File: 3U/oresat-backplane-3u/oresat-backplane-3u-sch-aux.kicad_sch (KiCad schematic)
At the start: 0 parts

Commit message: Added example aux connectors.
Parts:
- added CF2.1, CF3.1: SFM-110-01-S-D-LC, oresat-connectors:J-SAMTEC-CF-SFM-110-X1-XXX-D-LC, symbol oresat-connectors:J-SAMTEC-SFM-110-X1-XXX-D-LC
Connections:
- new net GND: CF2.1.LC1, CF2.1.LC2, CF3.1.LC1, CF3.1.LC2
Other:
- note added: "All capacitors 0603 >= 25V unless otherwise noted. All resistors 0603 1% unelss otherwise noted."
- note added: "NOTE: Aux connector is the Samtec SFM-110, which has an infinite variety of versions. For a discussion on those varieties, see"

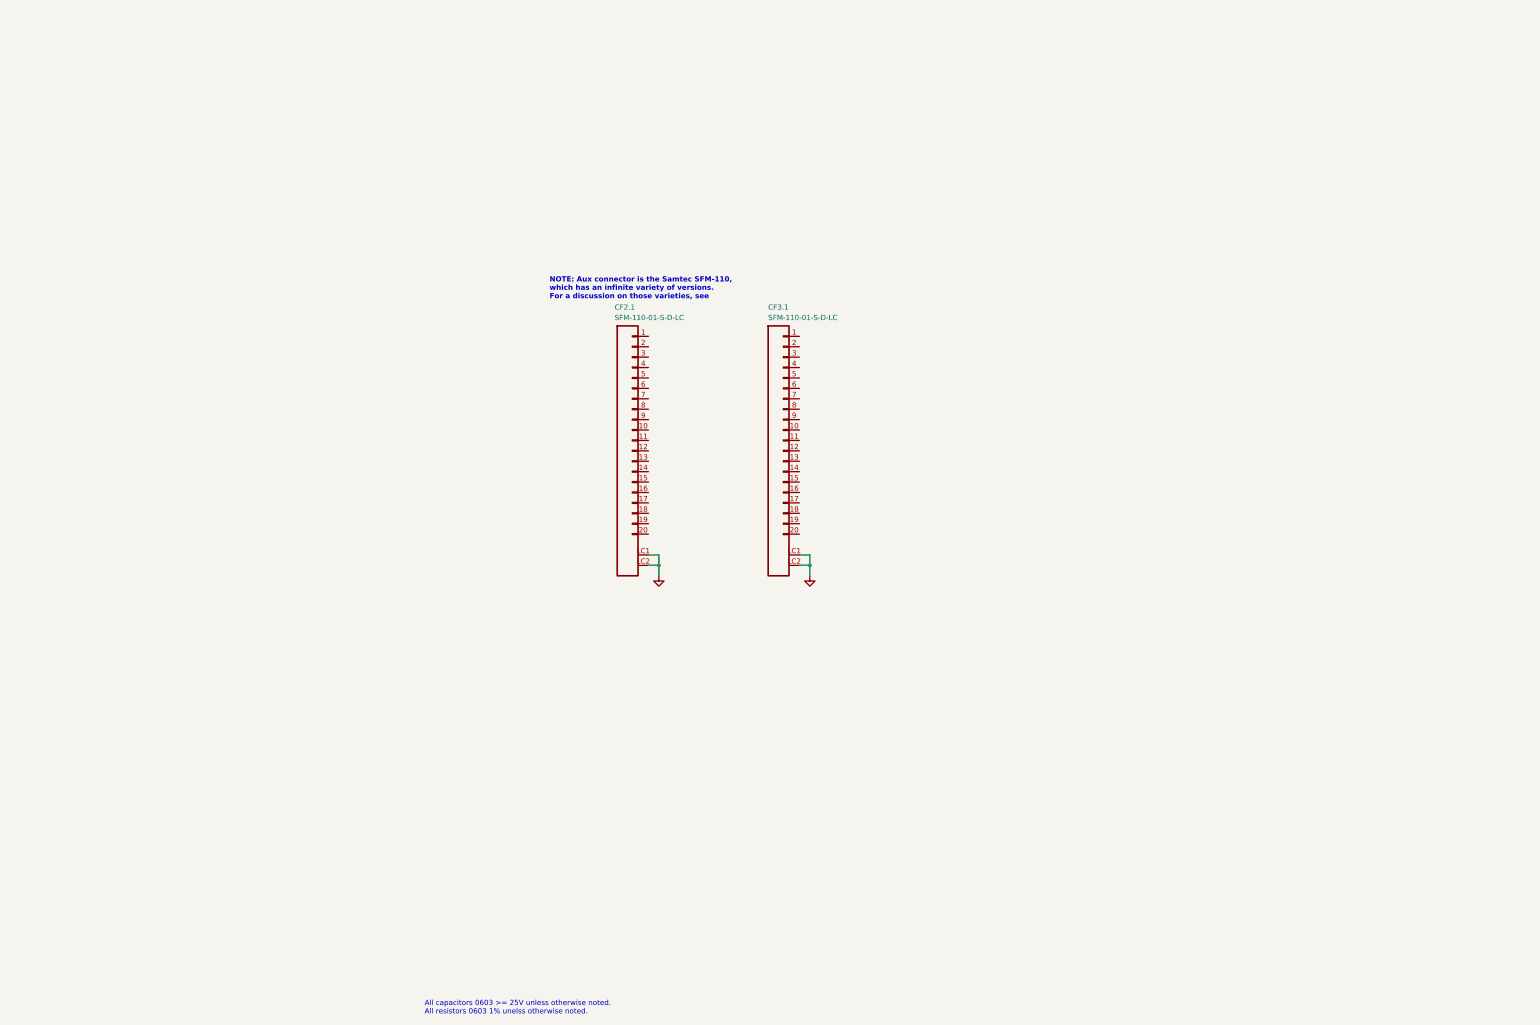
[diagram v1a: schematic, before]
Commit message: Added more Auxiliary connectors
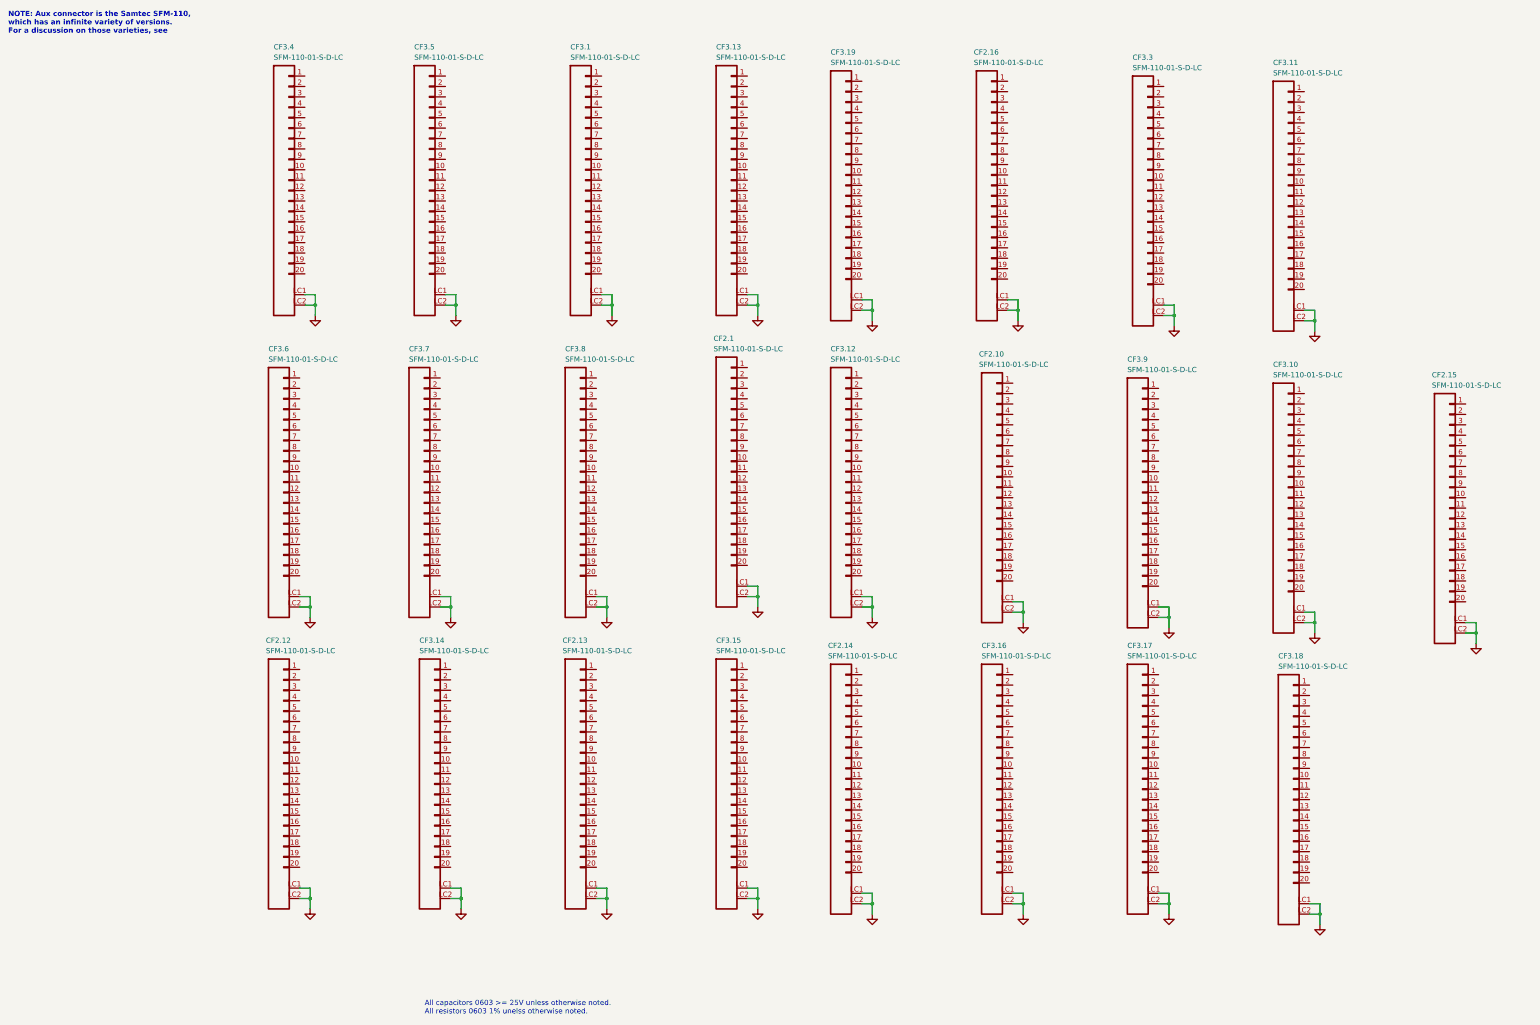
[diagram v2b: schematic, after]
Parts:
- added CF2.10, CF2.12, CF2.13, CF2.14, CF2.15, CF2.16, CF3.10, CF3.11, CF3.12, CF3.13, CF3.14, CF3.15, CF3.16, CF3.17, CF3.18, CF3.19, CF3.3, CF3.4, CF3.5, CF3.6, CF3.7, CF3.8, CF3.9: SFM-110-01-S-D-LC, oresat-connectors:J-SAMTEC-CF-SFM-110-X1-XXX-D-LC, symbol oresat-connectors:J-SAMTEC-SFM-110-X1-XXX-D-LC
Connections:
- net GND: now also CF2.10.LC1, CF2.10.LC2, CF2.12.LC1, CF2.12.LC2, CF2.13.LC1, CF2.13.LC2, CF2.14.LC1, CF2.14.LC2, CF2.15.LC1, CF2.15.LC2, CF2.16.LC1, CF2.16.LC2, CF3.10.LC1, CF3.10.LC2, CF3.11.LC1, CF3.11.LC2, CF3.12.LC1, CF3.12.LC2, CF3.13.LC1, CF3.13.LC2, CF3.14.LC1, CF3.14.LC2, CF3.15.LC1, CF3.15.LC2, CF3.16.LC1, CF3.16.LC2, CF3.17.LC1, CF3.17.LC2, CF3.18.LC1, CF3.18.LC2, CF3.19.LC1, CF3.19.LC2, CF3.3.LC1, CF3.3.LC2, CF3.4.LC1, CF3.4.LC2, CF3.5.LC1, CF3.5.LC2, CF3.6.LC1, CF3.6.LC2, CF3.7.LC1, CF3.7.LC2, CF3.8.LC1, CF3.8.LC2, CF3.9.LC1, CF3.9.LC2
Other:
- moved on the sheet: CF2.1, CF3.1

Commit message: Connectors laid out, unrouted
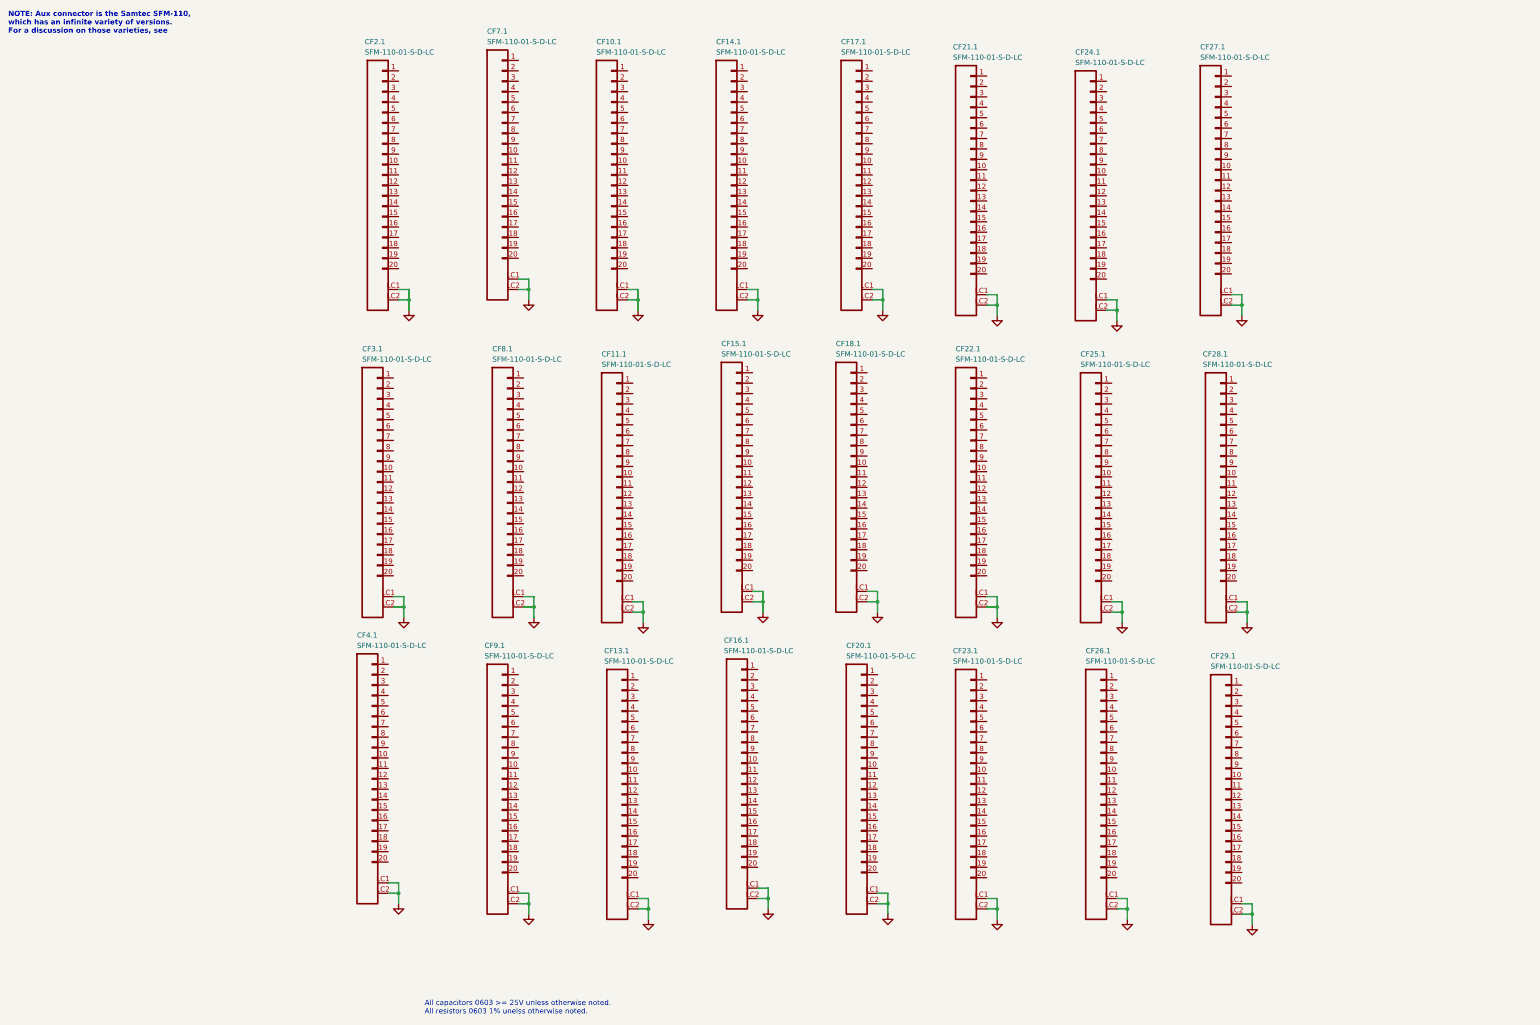
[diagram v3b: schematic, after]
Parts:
- removed CF3.14, CF3.17, CF3.18, CF3.6, CF3.7: SFM-110-01-S-D-LC, oresat-connectors:J-SAMTEC-CF-SFM-110-X1-XXX-D-LC, symbol oresat-connectors:J-SAMTEC-SFM-110-X1-XXX-D-LC
- added CF10.1, CF22.1, CF29.1, CF4.1: SFM-110-01-S-D-LC, oresat-connectors:J-SAMTEC-CF-SFM-110-X1-XXX-D-LC, symbol oresat-connectors:J-SAMTEC-SFM-110-X1-XXX-D-LC
- renumbered CF3.4 to CF11.1, CF2.13 to CF13.1, CF3.5 to CF14.1, CF3.8 to CF15.1, CF2.14 to CF16.1, CF3.13 to CF17.1, CF3.12 to CF18.1, CF3.19 to CF20.1, CF2.10 to CF21.1, CF2.16 to CF23.1, CF3.9 to CF24.1, CF3.10 to CF25.1, CF3.3 to CF26.1, CF3.11 to CF27.1, CF2.15 to CF28.1, CF3.15 to CF7.1, CF3.16 to CF8.1, CF2.12 to CF9.1
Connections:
- net GND: now also CF10.1.LC1, CF10.1.LC2, CF22.1.LC1, CF22.1.LC2, CF29.1.LC1, CF29.1.LC2, CF4.1.LC1, CF4.1.LC2
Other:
- moved on the sheet: CF11.1, CF13.1, CF14.1, CF15.1, CF16.1, CF17.1, CF18.1, CF2.1, CF20.1, CF21.1, CF23.1, CF24.1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

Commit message: Moved can lines to back & fixed RF schematic organization
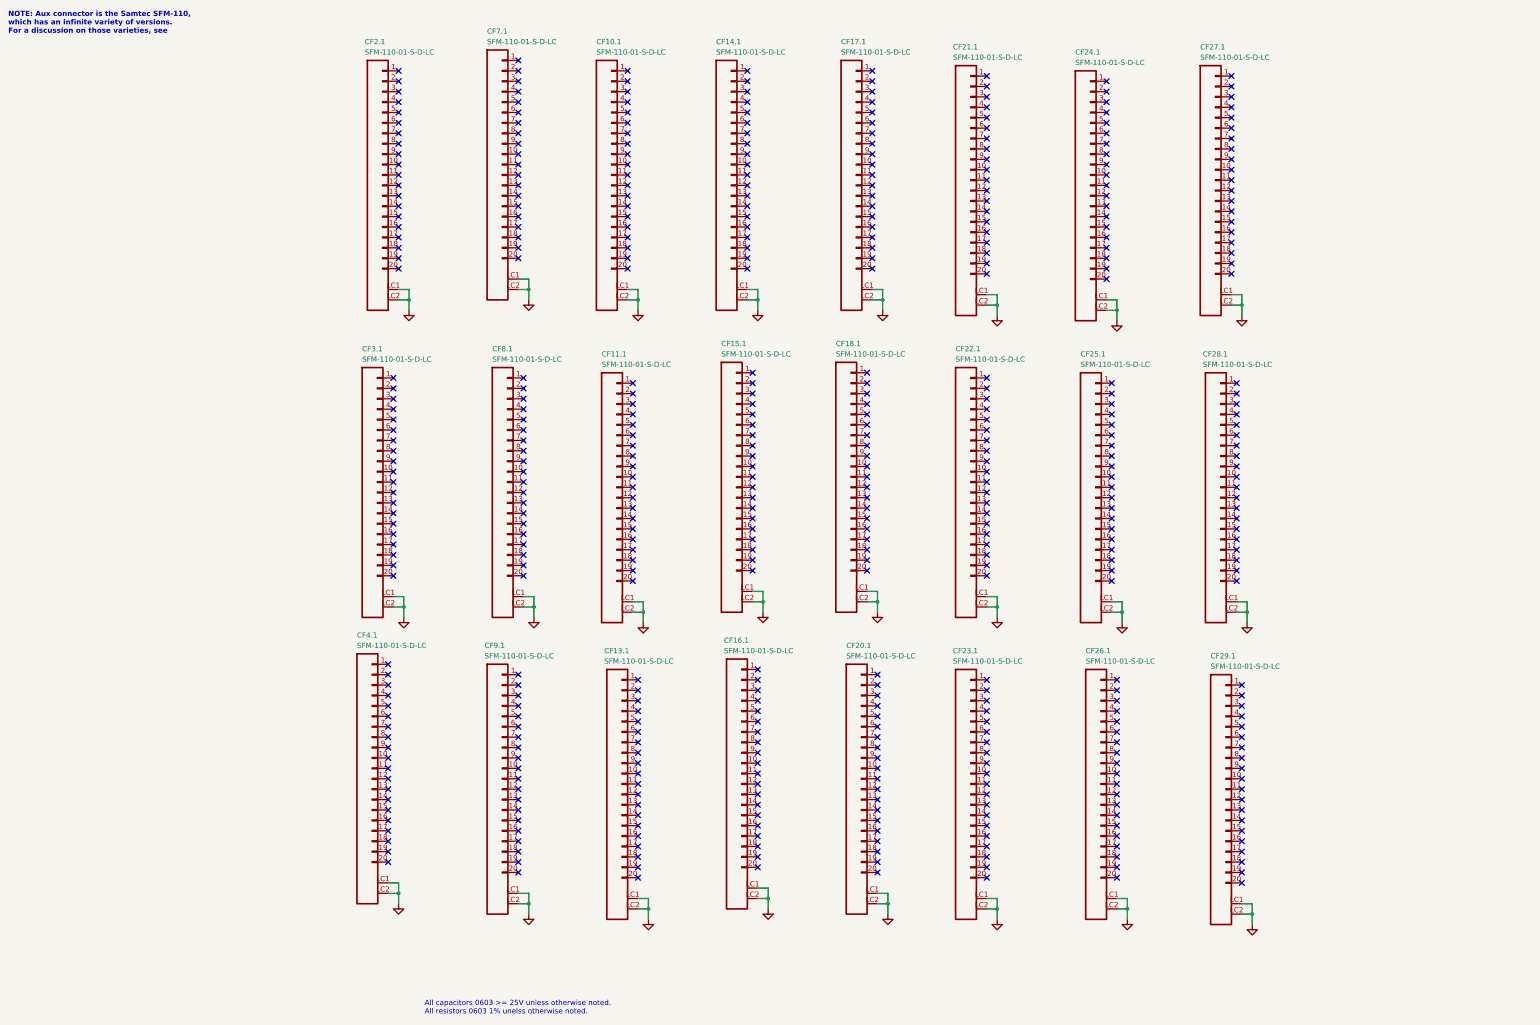
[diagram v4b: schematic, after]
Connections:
- no-connect marks 0 -> 480

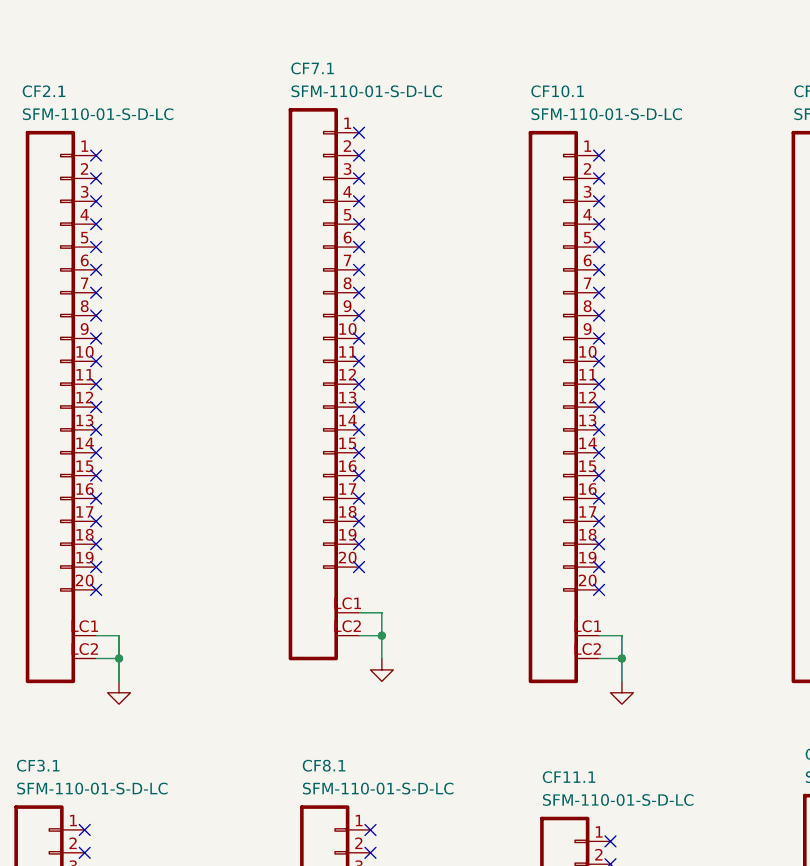
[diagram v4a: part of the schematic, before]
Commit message: Back solder mask added & can resistors moved to F.cu. Final
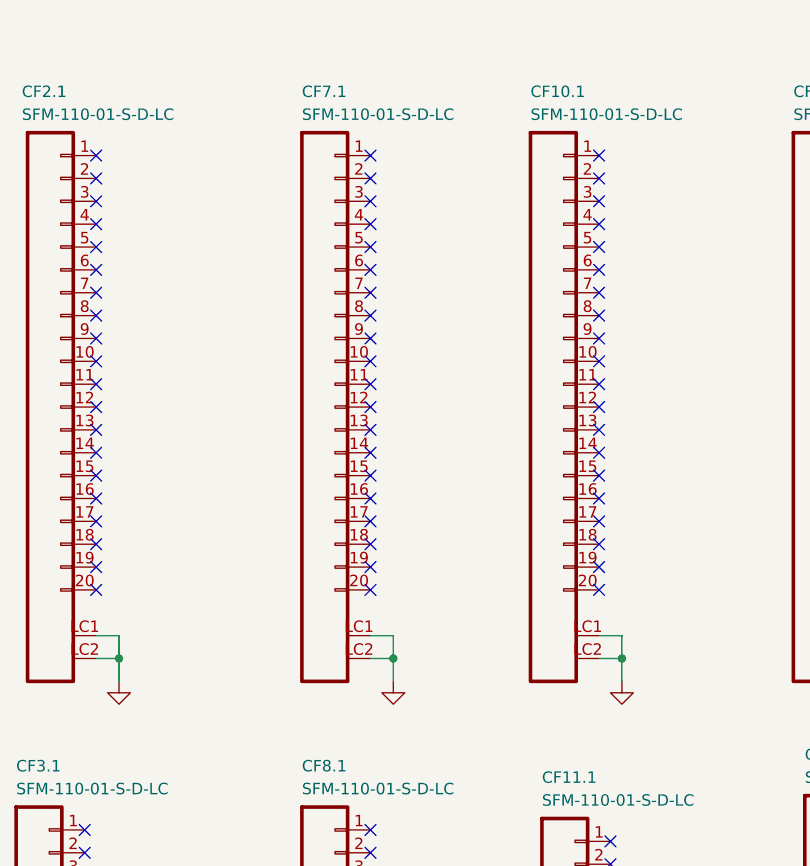
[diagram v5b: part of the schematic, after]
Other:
- moved on the sheet: CF7.1
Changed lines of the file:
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@@
 	)
 	(junction
-		(at 146.05 91.44)
+		(at 147.32 93.98)
 		(diameter 0)
 		(color 0 0 0 0)
@@
 	)
 	(no_connect
-		(at 143.51 53.34)
+		(at 144.78 55.88)
 	)
 	(no_connect
@@
 	)
 	(no_connect
-		(at 143.51 48.26)
+		(at 144.78 50.8)
 	)
 	(no_connect
@@
 	)
 	(no_connect
-		(at 143.51 81.28)
+		(at 144.78 83.82)
 	)
 	(no_connect
@@
 	)
 	(no_connect
-		(at 143.51 63.5)
+		(at 144.78 66.04)
 	)
 	(no_connect
@@
 	)
 	(no_connect
-		(at 143.51 78.74)
+		(at 144.78 81.28)
 	)
 	(no_connect
@@
 	)
 	(no_connect
-		(at 143.51 35.56)
+		(at 144.78 38.1)
 	)
 	(no_connect
@@
 	)
 	(no_connect
-		(at 143.51 66.04)
+		(at 144.78 68.58)
 	)
 	(no_connect
@@
 	)
 	(no_connect
-		(at 143.51 55.88)
+		(at 144.78 58.42)
 	)
 	(no_connect
@@
 	)
 	(no_connect
-		(at 143.51 60.96)
+		(at 144.78 63.5)
 	)
 	(no_connect
-		(at 143.51 38.1)
+		(at 144.78 40.64)
 	)
 	(no_connect
@@
 	)
 	(no_connect
-		(at 143.51 43.18)
+		(at 144.78 45.72)
 	)
 	(no_connect
@@
 	)
 	(no_connect
-		(at 143.51 40.64)
+		(at 144.78 43.18)
 	)
 	(no_connect
@@
 	)
 	(no_connect
-		(at 143.51 71.12)
+		(at 144.78 73.66)
 	)
 	(no_connect
@@
 	)
 	(no_connect
-		(at 143.51 45.72)
+		(at 144.78 48.26)
 	)
 	(no_connect
@@
 	)
 	(no_connect
-		(at 143.51 73.66)
+		(at 144.78 76.2)
 	)
 	(no_connect
@@
 	)
 	(no_connect
-		(at 143.51 50.8)
+		(at 144.78 53.34)
 	)
 	(no_connect
@@
 	)
 	(no_connect
-		(at 143.51 58.42)
+		(at 144.78 60.96)
 	)
 	(no_connect
@@
 	)
 	(no_connect
-		(at 143.51 68.58)
+		(at 144.78 71.12)
 	)
 	(no_connect
@@
 	)
 	(no_connect
-		(at 143.51 76.2)
+		(at 144.78 78.74)
 	)
 	(no_connect
@@
 	)
 	(no_connect
-		(at 143.51 83.82)
+		(at 144.78 86.36)
 	)
 	(no_connect
@@
 	(wire
 		(pts
-			(xy 146.05 91.44) (xy 146.05 88.9)
+			(xy 147.32 93.98) (xy 147.32 91.44)
 		)
 		(stroke
@@
 	(wire
 		(pts
-			(xy 146.05 93.98) (xy 146.05 91.44)
+			(xy 147.32 96.52) (xy 147.32 93.98)
 		)
 		(stroke
@@
 	(wire
 		(pts
-			(xy 146.05 88.9) (xy 143.51 88.9)
+			(xy 147.32 91.44) (xy 144.78 91.44)
 		)
 		(stroke
@@
 	(wire
 		(pts
-			(xy 146.05 91.44) (xy 143.51 91.44)
+			(xy 147.32 93.98) (xy 144.78 93.98)
 		)
 		(stroke
@@
 	(symbol
 		(lib_id "power:GND")
-		(at 146.05 93.98 0)
+		(at 147.32 96.52 0)
 		(unit 1)
 		(exclude_from_sim no)
@@
 		(dnp no)
 		(property "Reference" "#GND049"
-			(at 146.05 93.98 0)
+			(at 147.32 96.52 0)
 			(effects
 				(font
@@
 		)
 		(property "Value" "GND"
-			(at 146.05 93.98 0)
+			(at 147.32 96.52 0)
 			(effects
 				(font
@@
 		)
 		(property "Footprint" ""
-			(at 146.05 93.98 0)
+			(at 147.32 96.52 0)
 			(effects
 				(font
@@
 		)
 		(property "Datasheet" ""
-			(at 146.05 93.98 0)
+			(at 147.32 96.52 0)
 			(effects
 				(font
@@
 		)
 		(property "Description" ""
-			(at 146.05 93.98 0)
+			(at 147.32 96.52 0)
 			(effects
 				(font
@@
 	(symbol
 		(lib_id "oresat-connectors:J-SAMTEC-SFM-110-X1-XXX-D-LC")
-		(at 138.43 83.82 0)
+		(at 139.7 86.36 0)
 		(unit 1)
 		(exclude_from_sim no)
@@
 		(dnp no)
 		(property "Reference" "CF7.1"
-			(at 135.89 29.21 0)
+			(at 137.16 31.75 0)
 			(effects
 				(font
@@
 		)
 		(property "Value" "SFM-110-01-S-D-LC"
-			(at 135.89 31.75 0)
+			(at 137.16 34.29 0)
 			(effects
 				(font
@@
 		)
 		(property "Footprint" "oresat-connectors:J-SAMTEC-CF-SFM-110-X1-XXX-D-LC"
-			(at 143.51 143.51 0)
+			(at 144.78 146.05 0)
 			(effects
 				(font
@@
 		)
 		(property "Datasheet" "https://suddendocs.samtec.com/catalog_english/sfm.pdf"
-			(at 140.97 147.32 0)
+			(at 142.24 149.86 0)
 			(effects
 				(font
@@
 		)
 		(property "Description" "OreSat backplane connector, 2x20 RA"
-			(at 138.43 83.82 0)
+			(at 139.7 86.36 0)
 			(effects
 				(font
@@
 		)
 		(property "DIS" "DigiKey"
-			(at 138.43 83.82 0)
+			(at 139.7 86.36 0)
 			(effects
 				(font
@@
 		)
 		(property "DPN" "SFM-110-01-S-D-LC-ND"
-			(at 138.43 83.82 0)
+			(at 139.7 86.36 0)
 			(effects
 				(font
@@
 		)
 		(property "MFR" "Samtec Inc."
-			(at 138.43 83.82 0)
+			(at 139.7 86.36 0)
 			(effects
 				(font
@@
 		)
 		(property "MPN" "SFM-110-01-S-D-LC"
-			(at 138.43 83.82 0)
+			(at 139.7 86.36 0)
 			(effects
 				(font
